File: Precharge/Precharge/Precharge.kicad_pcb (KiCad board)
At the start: 2 copper layers, 133 x 98 mm, 119 parts, among them J1 MicroFit, J2 Mini-Fit_Jr_5566-04A, J3 Micro-Fit 43045-0212, K1 OMRON-G2RL-24, K2 G7L-2A-X-L, Q1 2N7002, Q2 MMBT3906, Q3 2N7002, U1 TJA1051T-3, U10 LM393, U11 4N35, U2 SPAN02A-12, U3 Teensy4.0, U4 LM1117-5.0, U5 4N35, U6 4N35, U7 LM331, U8 LM331, U9 LM2904

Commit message: :hammer: PCB artwork
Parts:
- added G***: LOGO, Precharge:electric-shock-symbol, F.Cu at (93.5, 116.5)
- added G***: LOGO, Precharge:logo, F.Cu at (197.0, 64.2)
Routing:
- added copper zone on B.Cu, net GLV-
- added copper zone on F.Cu, net GLV-
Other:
- outline, holes or cut-outs redrawn
- board text added: "CANH"
- board text added: "CANL"
- board text added: "DON'T PANIC"
- board text added: "GLV System"
- board text added: "GLV-"
- board text added: "HIGH VOLTAGE"
- board text added: "PDOC"
- board text added: "SHT DN IN"
- board text added: "SHT DN OUT"
- board text added: "STATUS"
- board text added: "STS"
- board text added: "TS-"
- board text added: "Tractive System"
- board text added: "github.com/michaelruppe"

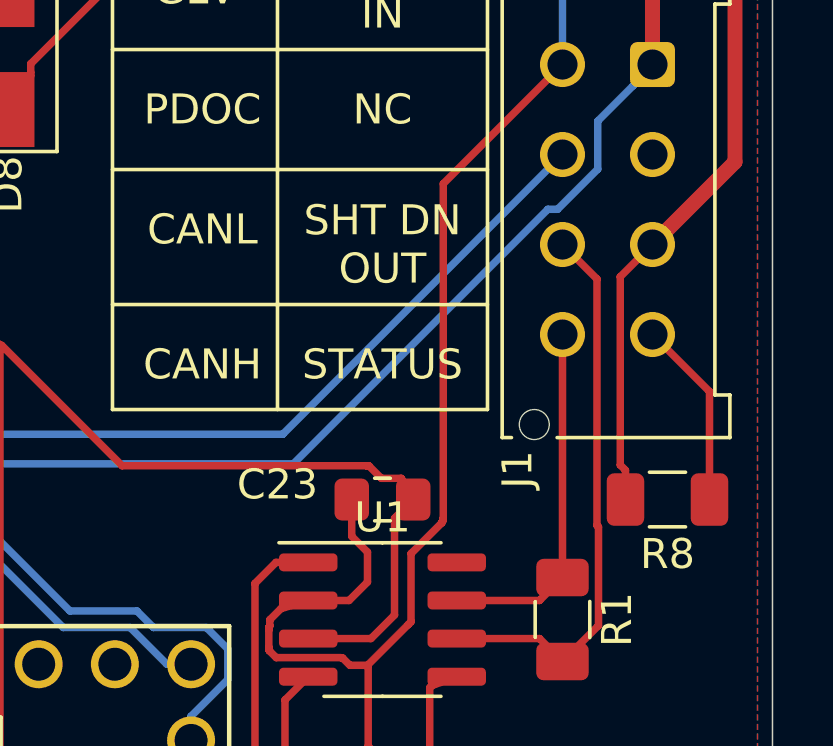
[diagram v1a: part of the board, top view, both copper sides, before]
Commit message: 🔩 Connect CAN transceiver S->GND
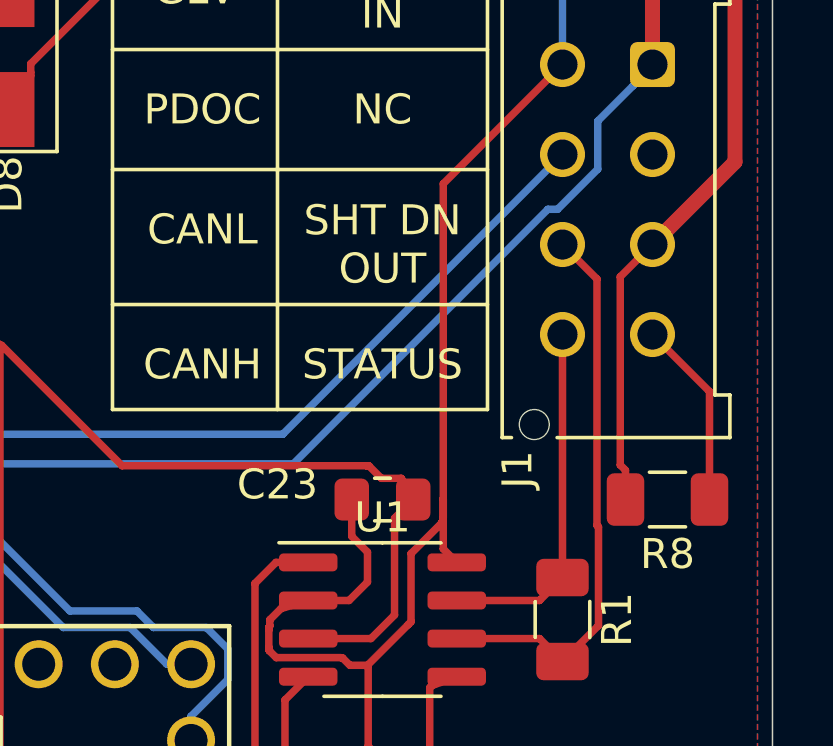
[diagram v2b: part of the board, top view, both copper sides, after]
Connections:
- U1 pad 8: (no net) -> GLV-
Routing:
- net GLV-: track 319.2 -> 321.5 mm
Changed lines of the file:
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@@
     (thickness 1.6)
     (drawings 54)
-    (tracks 1677)
+    (tracks 1680)
     (zones 0)
     (modules 121)
@@
     (add_net "Net-(D5-Pad2)")
     (add_net "Net-(D9-Pad2)")
+    (add_net "Net-(J1-Pad2)")
     (add_net "Net-(J2-Pad1)")
+    (add_net "Net-(J2-Pad2)")
+    (add_net "Net-(J2-Pad3)")
+    (add_net "Net-(K1-Pad2)")
+    (add_net "Net-(K1-Pad7)")
     (add_net "Net-(K2-Pad4)")
     (add_net "Net-(Q1-Pad1)")
@@
     (add_net "Net-(R40-Pad2)")
     (add_net "Net-(R41-Pad2)")
+    (add_net "Net-(U10-Pad7)")
+    (add_net "Net-(U11-Pad3)")
+    (add_net "Net-(U11-Pad6)")
+    (add_net "Net-(U2-Pad3)")
+    (add_net "Net-(U2-Pad5)")
+    (add_net "Net-(U2-Pad8)")
+    (add_net "Net-(U3-Pad11)")
+    (add_net "Net-(U3-Pad12)")
+    (add_net "Net-(U3-Pad15)")
+    (add_net "Net-(U3-Pad16)")
+    (add_net "Net-(U3-Pad18)")
+    (add_net "Net-(U3-Pad19)")
+    (add_net "Net-(U3-Pad20)")
+    (add_net "Net-(U3-Pad23)")
+    (add_net "Net-(U3-Pad24)")
+    (add_net "Net-(U3-Pad26)")
+    (add_net "Net-(U3-Pad27)")
+    (add_net "Net-(U3-Pad29)")
+    (add_net "Net-(U3-Pad30)")
+    (add_net "Net-(U3-Pad34)")
+    (add_net "Net-(U3-Pad35)")
+    (add_net "Net-(U3-Pad36)")
+    (add_net "Net-(U3-Pad37)")
+    (add_net "Net-(U3-Pad38)")
+    (add_net "Net-(U3-Pad39)")
+    (add_net "Net-(U3-Pad40)")
+    (add_net "Net-(U3-Pad41)")
+    (add_net "Net-(U3-Pad42)")
+    (add_net "Net-(U3-Pad43)")
+    (add_net "Net-(U3-Pad44)")
+    (add_net "Net-(U5-Pad3)")
+    (add_net "Net-(U5-Pad6)")
+    (add_net "Net-(U6-Pad3)")
+    (add_net "Net-(U6-Pad6)")
   )
   (module Precharge:electric-shock-symbol locked (layer F.Cu)
@@
     (fp_line (start 0 2.56) (end -1.95 2.56) (layer F.SilkS) (width 0.12))
     (fp_line (start 0 2.56) (end 1.95 2.56) (layer F.SilkS) (width 0.12))
-    (pad 8 smd roundrect (at 2.475 -1.905) (size 1.95 0.6) (layers F.Cu F.Paste F.Mask) (roundrect_rratio 0.25))
+    (pad 8 smd roundrect (at 2.475 -1.905) (size 1.95 0.6) (layers F.Cu F.Paste F.Mask) (roundrect_rratio 0.25)
+      (net 8 GLV-))
     (pad 7 smd roundrect (at 2.475 -0.635) (size 1.95 0.6) (layers F.Cu F.Paste F.Mask) (roundrect_rratio 0.25)
       (net 56 /CANH))
@@
   (segment (start 150.5201 127.0047) (end 150.5201 126.2377) (width 0.25) (layer F.Cu) (net 8))
   (segment (start 194 90) (end 190.0261 93.9739) (width 0.25) (layer F.Cu) (net 8) (status 10))
-  (segment (start 190.0261 93.9739) (end 190.0261 105.1261) (width 0.25) (layer F.Cu) (net 8))
   (segment (start 190.0261 105.1261) (end 190.0241 105.1281) (width 0.25) (layer F.Cu) (net 8))
   (segment (start 190.0241 105.1281) (end 190.0241 105.1479) (width 0.25) (layer F.Cu) (net 8))
@@
   (segment (start 168.92 143.01) (end 181.62 143.01) (width 0.25) (layer B.Cu) (net 8) (status 20))
   (via (at 194.6523 80.0499) (size 0.8) (layers F.Cu B.Cu) (net 8))
+  (segment (start 190.0261 106.1461) (end 190.475 106.595) (width 0.25) (layer F.Cu) (net 8))
+  (segment (start 190.0261 104.4739) (end 190.0261 106.1461) (width 0.25) (layer F.Cu) (net 8))
+  (segment (start 190.0261 93.9739) (end 190.0261 104.4739) (width 0.25) (layer F.Cu) (net 8))
+  (segment (start 190.0261 104.4739) (end 190.0261 105.1261) (width 0.25) (layer F.Cu) (net 8))
   (segment (start 197 83.5) (end 198.4 83.5) (width 0.5) (layer F.Cu) (net 9) (status 10))
   (segment (start 198.4 83.5) (end 198.75 83.15) (width 0.5) (layer F.Cu) (net 9))
@@
   (segment (start 81.0749 128.5903) (end 85.6046 133.12) (width 0.25) (layer F.Cu) (net 10))
   (segment (start 85.6046 133.12) (end 92.5 133.12) (width 0.25) (layer F.Cu) (net 10))
-  (segment (start 74.5 130.5) (end 74.5 133.5) (width 0.5) (layer B.Cu) (net 72) (status 30))
   (segment (start 94.475 134.5) (end 92.5 134.5) (width 0.25) (layer B.Cu) (net 10) (status 10))
   (segment (start 92.5 134.5) (end 90 137) (width 0.25) (layer B.Cu) (net 10))
@@
   (segment (start 183.75 107.295) (end 184.45 106.595) (width 0.25) (layer F.Cu) (net 71))
   (segment (start 184.45 106.595) (end 185.525 106.595) (width 0.25) (layer F.Cu) (net 71) (status 20))
+  (segment (start 74.5 130.5) (end 74.5 133.5) (width 0.5) (layer B.Cu) (net 72) (status 30))
   (segment (start 74.5 132) (end 79.6 132) (width 0.5) (layer B.Cu) (net 72) (status 20))
   (via (at 103.5 131) (size 0.8) (drill 0.4) (layers F.Cu B.Cu) (net 72))

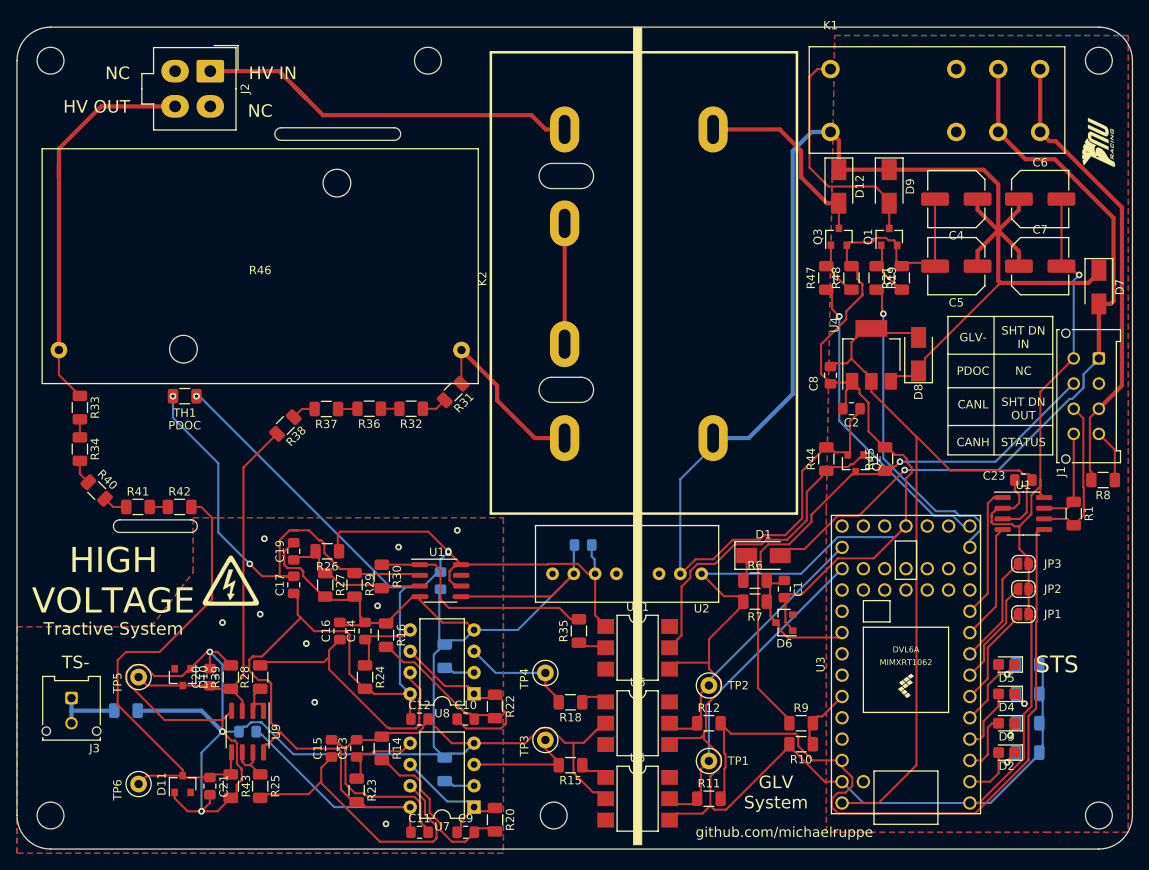
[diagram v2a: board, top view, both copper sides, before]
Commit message: :hammer: Add PCB artwork for status LEDs
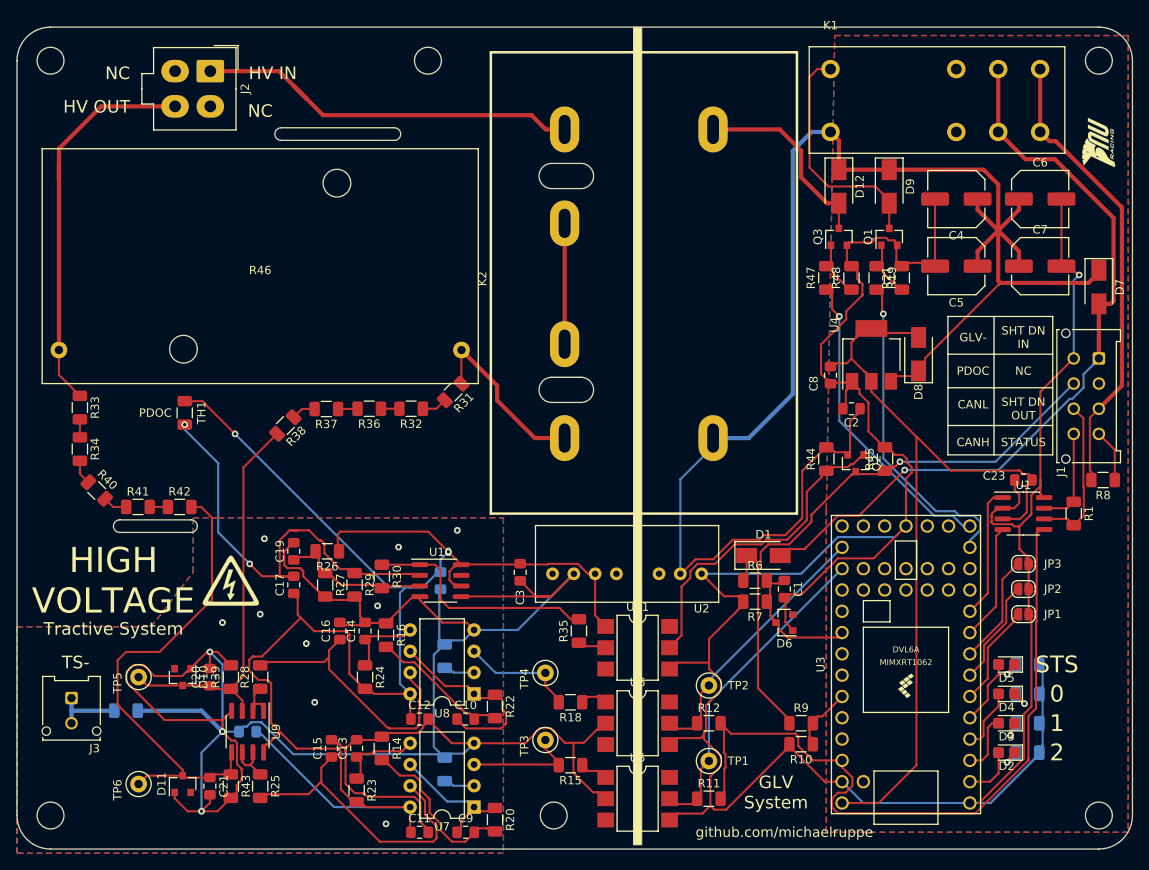
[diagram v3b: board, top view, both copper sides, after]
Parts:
- C3: moved to F.Cu
- moved C3 8.17 mm to (128.0, 115.5), turned to 90 degrees
- moved TH1 2.00 mm to (88.0, 96.5), turned to 90 degrees
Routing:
- net Net-(C17-Pad2): track 56.6 -> 52.6 mm
- net GNDS: track 282.4 -> 283.4 mm
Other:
- board text added: "0"
- board text added: "1"
- board text added: "2"
